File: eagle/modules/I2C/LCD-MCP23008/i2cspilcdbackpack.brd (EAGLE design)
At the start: 80 x 47.9 mm, 17 parts, among them IC1 MCP2300X/P, J2 RJ12RIGHTANGLE-I2C, J3 RJ12RIGHTANGLE-I2C

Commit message: Update
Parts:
- added X1: HD44780LCD-1602, adafruit:LCD1602
- C2: device adafruit:C0805K -> adafruit:C1206
- R1, R2, R3, R4, R5, R7: device adafruit:R0805 -> adafruit:M1206
- moved Q1 41.9 mm to (45.7, 26.8)
- moved C1 36.5 mm to (7.24, 21.7), turned to 0 degrees
- moved R7 35.5 mm to (41.9, 36.8)
- moved R6 34.3 mm to (44.5, 7.62), turned to 270 degrees
- moved R5 30.1 mm to (38.1, 36.8), turned to 90 degrees
- moved C2 28.6 mm to (7.37, 25.3), turned to 180 degrees
- moved R4 24.5 mm to (34.3, 36.8), turned to 90 degrees
- moved JP1 23.2 mm to (25.1, 16.7), turned to 0 degrees
- moved R1 20.2 mm to (30.5, 36.8), turned to 270 degrees
- moved R2 17.6 mm to (26.7, 36.8), turned to 270 degrees
- moved R3 17.2 mm to (23.0, 36.8), turned to 270 degrees
- moved J2 15.4 mm to (10.2, 4.45)
- moved J3 14.1 mm to (27.9, 4.45)
- moved A2 11.5 mm to (15.2, 36.8), turned to 270 degrees
- moved A1 8.52 mm to (11.4, 36.8), turned to 270 degrees
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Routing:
- net GND: track 0.00 -> 150.5 mm
- net VCC: track 0.00 -> 112.0 mm, vias 0 -> 1
- net CLOCK: track 0.00 -> 77.5 mm, vias 0 -> 2
- net DATA: track 0.00 -> 74.2 mm, vias 0 -> 1
- net N$10: track 0.00 -> 42.1 mm
- net N$2: track 0.00 -> 34.1 mm, vias 0 -> 1
- net LITE: track 0.00 -> 31.9 mm
- net N$4: track 0.00 -> 26.8 mm, vias 0 -> 1
- net N$11: track 0.00 -> 26.5 mm
- net N$3: track 0.00 -> 26.3 mm, vias 0 -> 1
- net N$1: track 0.00 -> 25.1 mm, vias 0 -> 2
- net N$7: track 0.00 -> 13.2 mm, vias 0 -> 1
- net DB5: track 0.00 -> 11.8 mm
- net DB6: track 0.00 -> 11.7 mm
- net DB4: track 0.00 -> 11.7 mm
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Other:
- board size 80 x 47.9 mm -> 52.1 x 43.2 mm
- board text added: "10uF polarised ?"
- board text added: "equivalent transistor"
- board text removed: "A0"
- board text removed: "A1"
- board text removed: "A2"

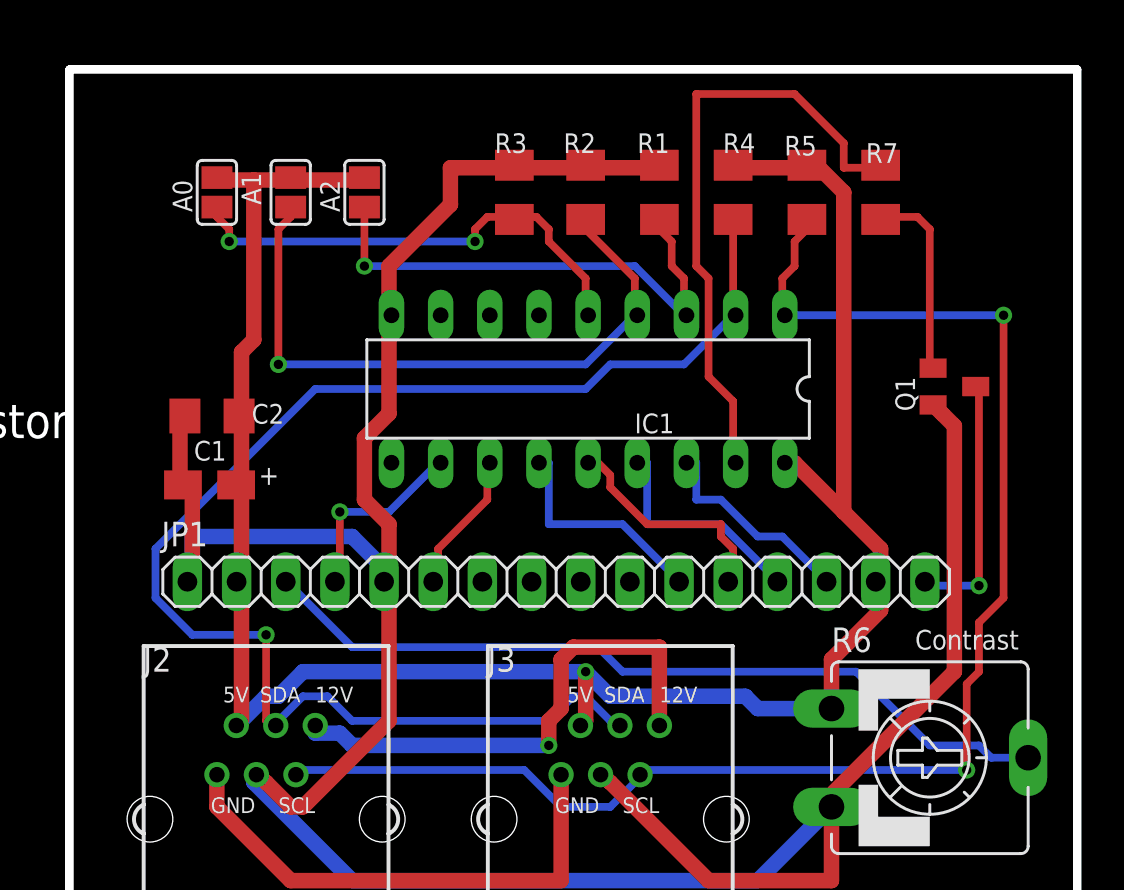
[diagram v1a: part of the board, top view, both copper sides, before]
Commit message: Remove via close to rj12
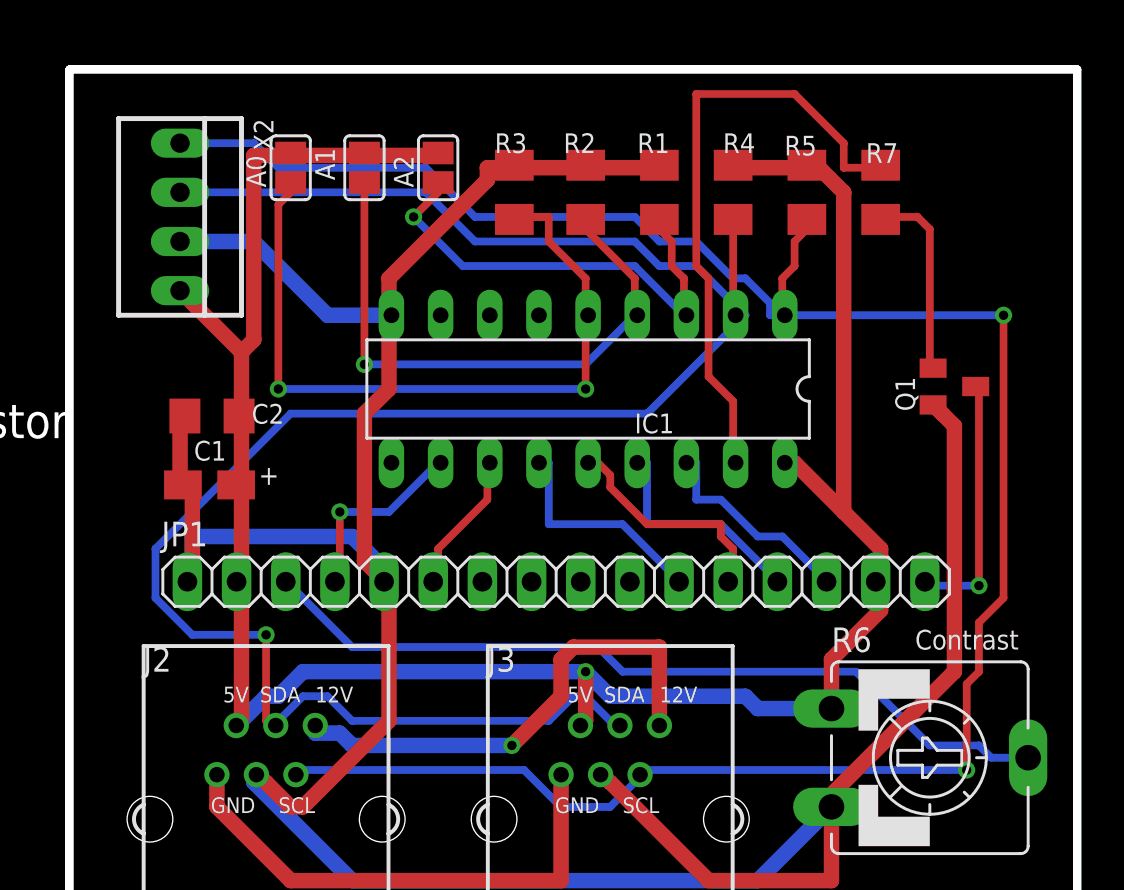
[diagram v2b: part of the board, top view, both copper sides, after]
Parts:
- added X2: 22-23-2041, con-molex:22-23-2041
- moved A1 4.02 mm to (15.2, 38.1)
- moved A2 4.02 mm to (19.1, 38.1)
- moved A0 4.02 mm to (11.4, 38.1)
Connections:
- net CLOCK: now also X2.1
- net DATA: now also X2.2
- net GND: now also X2.3
- net VCC: now also X2.4
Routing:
- net CLOCK: track 77.5 -> 112.8 mm
- net DATA: track 74.2 -> 107.0 mm
- net N$1: track 25.1 -> 38.4 mm
- net GND: track 150.5 -> 161.7 mm
- net VCC: track 112.0 -> 119.6 mm
- net N$2: track 34.1 -> 30.7 mm
- net N$3: track 26.3 -> 24.1 mm
- net N$4: track 26.8 -> 25.7 mm

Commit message: update
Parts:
- moved X1 4.02 mm to (101.6, 89.5)
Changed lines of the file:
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@@
 <element name="J3" library="lpatiny" package="RJ12-RIGHTANGLE-I2C" value="RJ12RIGHTANGLE-I2C" x="27.94" y="4.445"/>
 <element name="R6" library="pot" package="CA9V" value="" x="44.45" y="7.62" rot="R270"/>
-<element name="X1" library="adafruit" package="LCD1602" value="HD44780LCD-1602" x="105.41" y="90.805" rot="R180"/>
+<element name="X1" library="adafruit" package="LCD1602" value="HD44780LCD-1602" x="101.6" y="89.535" rot="R180"/>
 <element name="X2" library="con-molex" package="22-23-2041" value="22-23-2041" x="5.715" y="35.56" rot="R270">
 <attribute name="OC_NEWARK" value="38C0355" x="5.715" y="35.56" size="1.778" layer="27" rot="R270" display="off"/>
